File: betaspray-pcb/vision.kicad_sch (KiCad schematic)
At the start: 2 parts, among them J10 Conn_01x09_Pin, J8 Conn_01x09_Pin

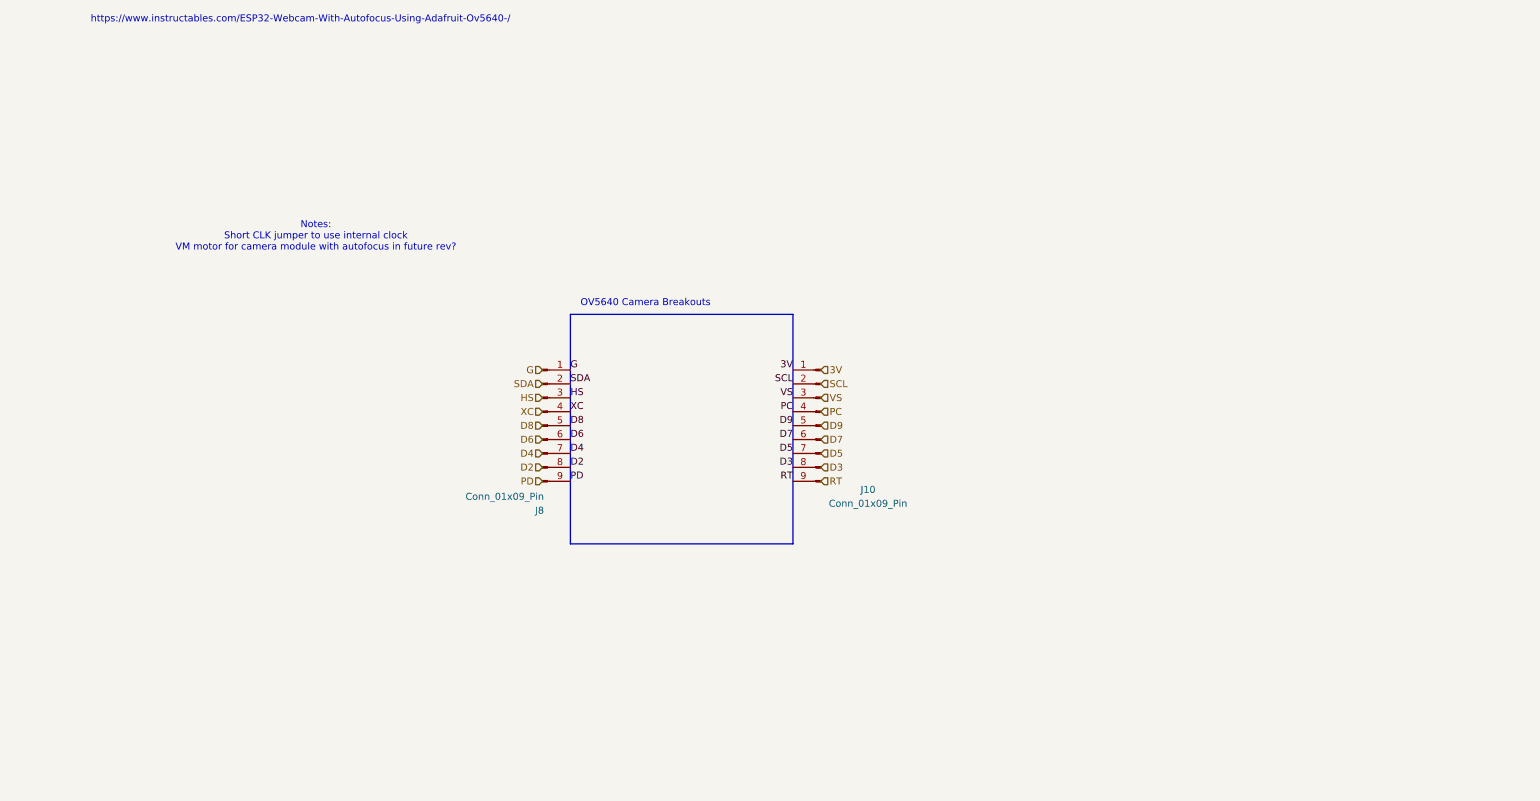
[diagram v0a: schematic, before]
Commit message: Added images and notes for wiring recommendations for vision subsys
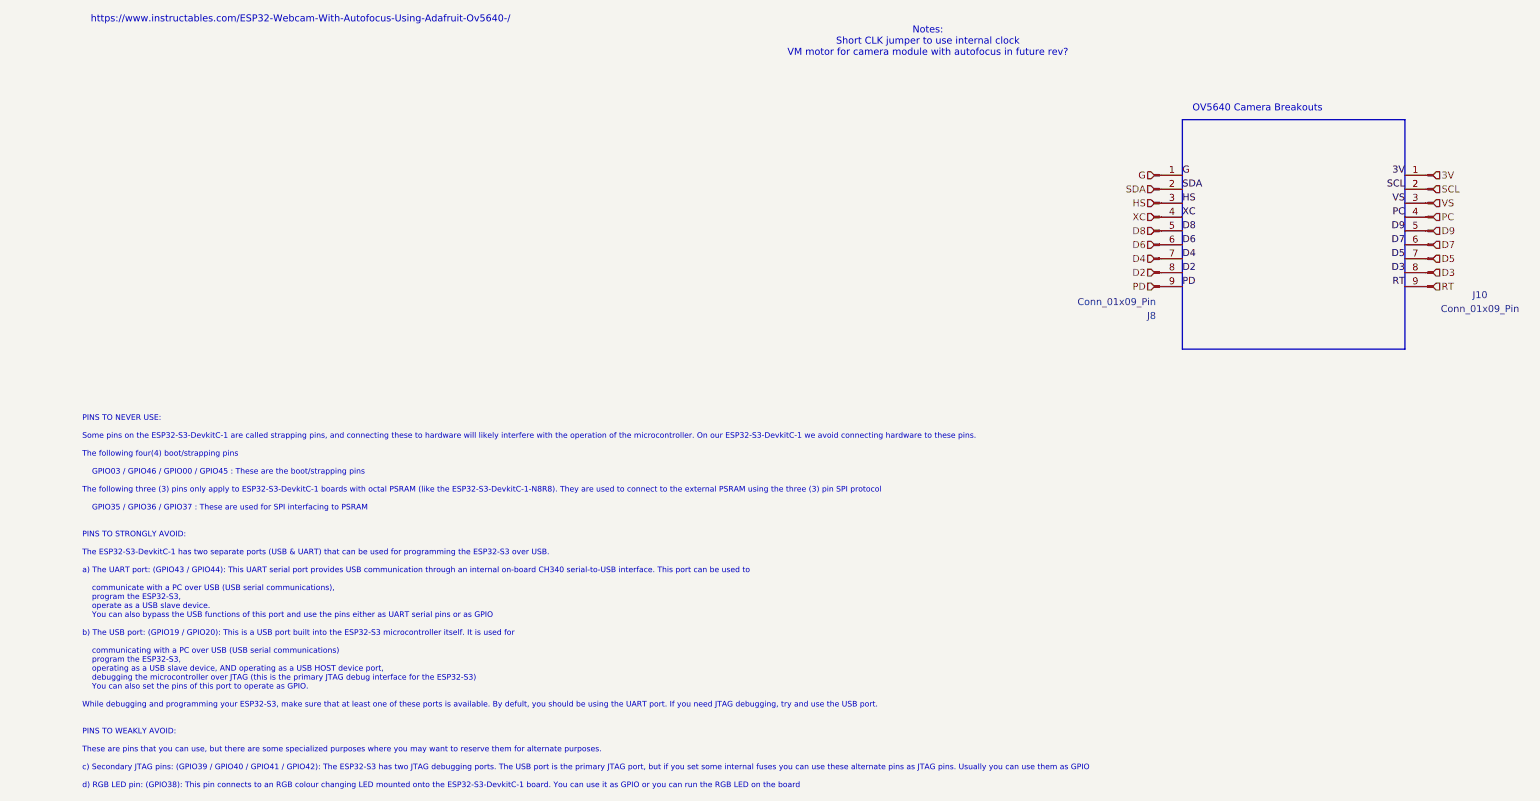
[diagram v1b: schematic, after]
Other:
- note added: "PINS TO NEVER USE: Some pins on the ESP32-S3-DevkitC-1 are called strapping pins, and connecting these to hardware will likely interfere with the operation of the microcontroller. On our ESP32-S3-DevkitC-1 we avoid connecting hardware to these pins. The following four(4) boot/strapping pins GPIO03 / GPIO46 / GPIO00 / GPIO45 : These are the boot/strapping pins The following three (3) pins only app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"
- moved on the sheet: J10, J8

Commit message: Connected Servo labels, added debug led
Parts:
- J10, J8: symbol betaspray_Connector:Conn_01x09_Pin -> betaspray_MCU_Espressif:Conn_01x09_Pin
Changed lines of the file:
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@@
 	)
 	(symbol
-		(lib_id "betaspray_Connector:Conn_01x09_Pin")
+		(lib_id "betaspray_MCU_Espressif:Conn_01x09_Pin")
 		(at 217.17 57.15 0)
 		(unit 1)
@@
 	)
 	(symbol
-		(lib_id "betaspray_Connector:Conn_01x09_Pin")
+		(lib_id "betaspray_MCU_Espressif:Conn_01x09_Pin")
 		(at 267.97 57.15 0)
 		(mirror y)

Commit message: Started layout
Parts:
- J10, J8: footprint (none) -> Connector_TE-Connectivity:TE_826576-9_1x09_P3.96mm_Vertical
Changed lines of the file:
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@@
 			)
 		)
-		(property "Footprint" ""
+		(property "Footprint" "Connector_TE-Connectivity:TE_826576-9_1x09_P3.96mm_Vertical"
 			(at 217.17 57.15 0)
 			(effects
@@
 			)
 		)
-		(property "Footprint" ""
+		(property "Footprint" "Connector_TE-Connectivity:TE_826576-9_1x09_P3.96mm_Vertical"
 			(at 267.97 57.15 0)
 			(effects

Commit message: fixed footprint
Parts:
- J10, J8: footprint Connector_TE-Connectivity:TE_826576-9_1x09_P3.96mm_Vertical -> Connector_PinHeader_2.54mm:PinHeader_1x09_P2.54mm_Vertical
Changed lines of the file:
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@@
 			)
 		)
-		(property "Footprint" "Connector_TE-Connectivity:TE_826576-9_1x09_P3.96mm_Vertical"
+		(property "Footprint" "Connector_PinHeader_2.54mm:PinHeader_1x09_P2.54mm_Vertical"
 			(at 217.17 57.15 0)
 			(effects
@@
 			)
 		)
-		(property "Footprint" "Connector_TE-Connectivity:TE_826576-9_1x09_P3.96mm_Vertical"
+		(property "Footprint" "Connector_PinHeader_2.54mm:PinHeader_1x09_P2.54mm_Vertical"
 			(at 267.97 57.15 0)
 			(effects
